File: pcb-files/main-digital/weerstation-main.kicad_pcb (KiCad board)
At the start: 2 copper layers, 100 x 100 mm, 43 parts, among them J1 sds011 pm10 pm2.5 dust sensor, J10 PCA9685, J11 rotatie as5600, J12 rotatie as5600, J13 rotatie as5600 2, J14 rotatie as5600 2, J15 rotatie as5600 2, J16 analoog bord connector, J17 rotatie as5600 3, J18 rotatie as5600 3, J19 rotatie as5600 3, J2 analoog bord connector (digit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, J20 rotatie as5600 4, J21 rotatie as5600 4, J22 rotatie as5600 4, J23 temp sensor AM2315C, J24 veml 7700, J25 VL53L0X, J26 hc-sr04, J27 ens160+aht21, J28 regenmeter digitaal flip sens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, J29 mpu-9265, J3 ina226, J30 ina226, J31 levelshift lv, J32 digitaal bord connector power, J33 servo, J34 levelshift hv, J35 servo_power, J4 bme280, J5 ina226, J6 rotatie as5600, J7 ina226, J8 ina226, J9 mpu-9265, U1 ESP32-DEVKIT-V1, U3 TCA9548A

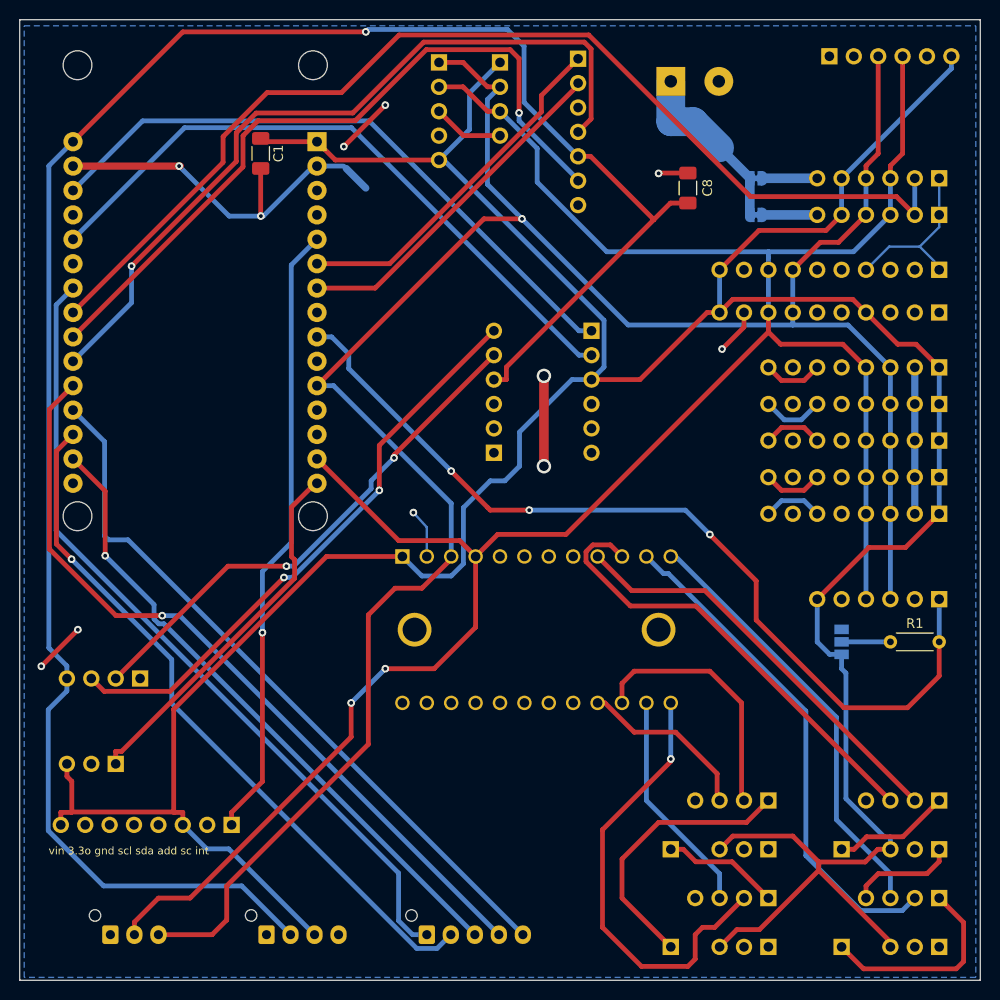
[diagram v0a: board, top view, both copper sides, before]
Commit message: update pcb files better layout and grounding inproved
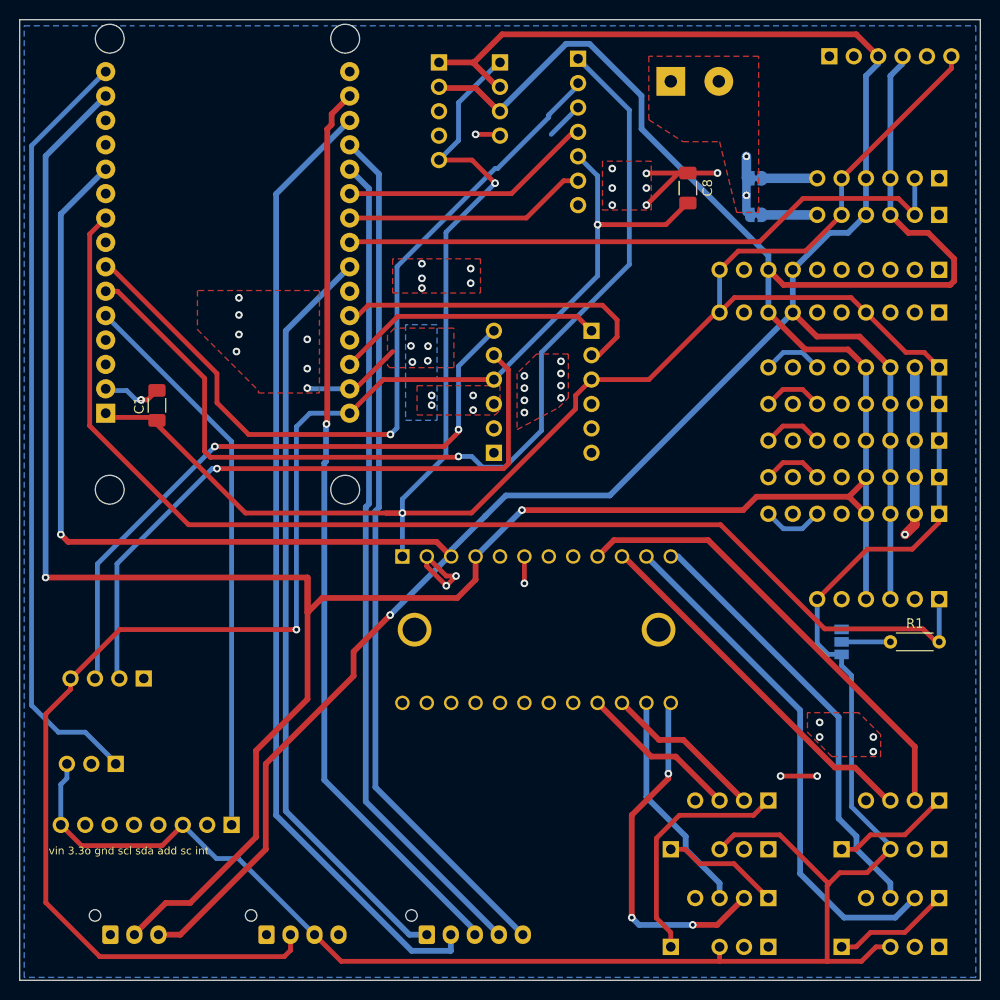
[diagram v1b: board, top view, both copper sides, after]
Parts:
- added H1: MountingHole, MountingHole:MountingHole_long, F.Cu at (25.7, 17.3)
- added H10: MountingHole, MountingHole:MountingHole_long, F.Cu at (45.0, 20.1)
- added H11: MountingHole, MountingHole:MountingHole_long, F.Cu at (45.0, 17.0)
- added H12: MountingHole, MountingHole:MountingHole_long, F.Cu at (45.0, 14.0)
- added H2: MountingHole, MountingHole:MountingHole_long, F.Cu at (25.7, 20.3)
- added H3: MountingHole, MountingHole:MountingHole_long, F.Cu at (27.2, 22.4)
- added H4: MountingHole, MountingHole:MountingHole_long, F.Cu at (25.7, 14.0)
- added H5: MountingHole, MountingHole:MountingHole_long, F.Cu at (34.3, 22.4)
- added H6: MountingHole, MountingHole:MountingHole_long, F.Cu at (41.1, 22.4)
- added H7: MountingHole, MountingHole:MountingHole_long, F.Cu at (37.6, 22.4)
- added H8: MountingHole, MountingHole:MountingHole_long, F.Cu at (30.7, 22.4)
- added H9: MountingHole, MountingHole:MountingHole_long, F.Cu at (44.2, 22.4)
- J10: value PCA9685 -> PCA9685 servo controller
- J33: value servo -> PCA9685 servo controller
- moved C1 28.4 mm to (27.8, 52.9), turned to 90 degrees
- moved U1 4.38 mm to (35.2, 38.2), turned to 0 degrees
- moved J26 0.38 mm to (26.4, 81.3)
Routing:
- net scl: track 238.8 -> 337.9 mm
- net tx0: track 37.0 -> 103.8 mm, vias 0 -> 1
- net sda: track 234.9 -> 301.3 mm, vias 1 -> 2
- net GND: track 126.4 -> 70.8 mm, vias 11 -> 47
- net 2.5um: track 81.2 -> 26.4 mm, vias 1 -> 0
- net 1um: track 76.4 -> 25.4 mm, vias 1 -> 0
- net Net-(J10-Pin_2): track 112.7 -> 65.2 mm
- net rx0: track 36.1 -> 83.5 mm, vias 0 -> 1
- net +5V: track 209.5 -> 164.0 mm, vias 1 -> 2
- net Net-(J28-Pin_1): track 38.6 -> 80.5 mm
- net lv1: track 66.0 -> 27.9 mm
- net +3.3V: track 368.4 -> 404.5 mm, vias 0 -> 2
- net lv2: track 68.6 -> 34.2 mm
- net Net-(J25-Pin_1): track 93.4 -> 124.5 mm, vias 3 -> 0
- net ADC3 alert: track 67.2 -> 94.9 mm
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- added copper zone on F.Cu, net +5VL
- added copper zone on F.Cu, net GND

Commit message: pcbs as orderd. loads of grounding fixes
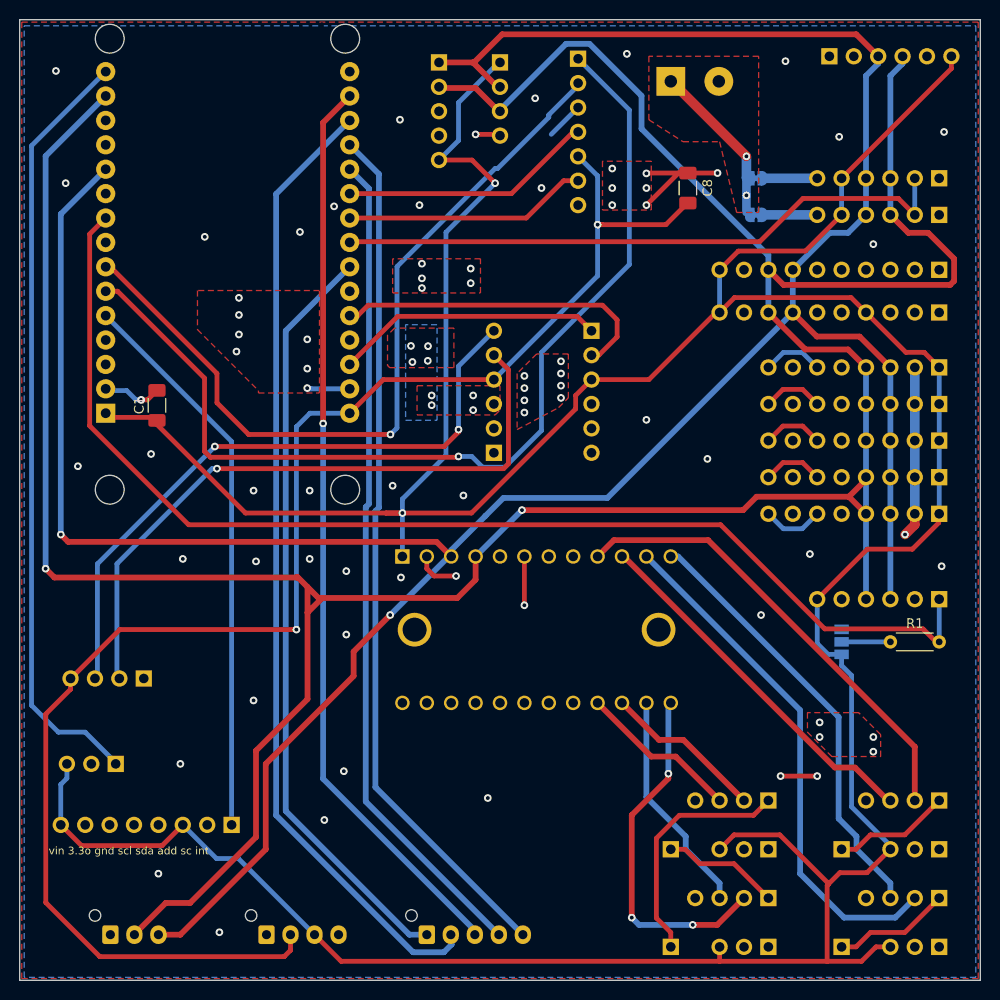
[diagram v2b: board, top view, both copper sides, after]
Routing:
- net +5VL: track 6.27 -> 17.4 mm
- net GND: track 70.8 -> 63.0 mm, vias 47 -> 84
- net scl: track 337.9 -> 335.2 mm
